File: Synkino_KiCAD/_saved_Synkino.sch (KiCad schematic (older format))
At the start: 101 parts

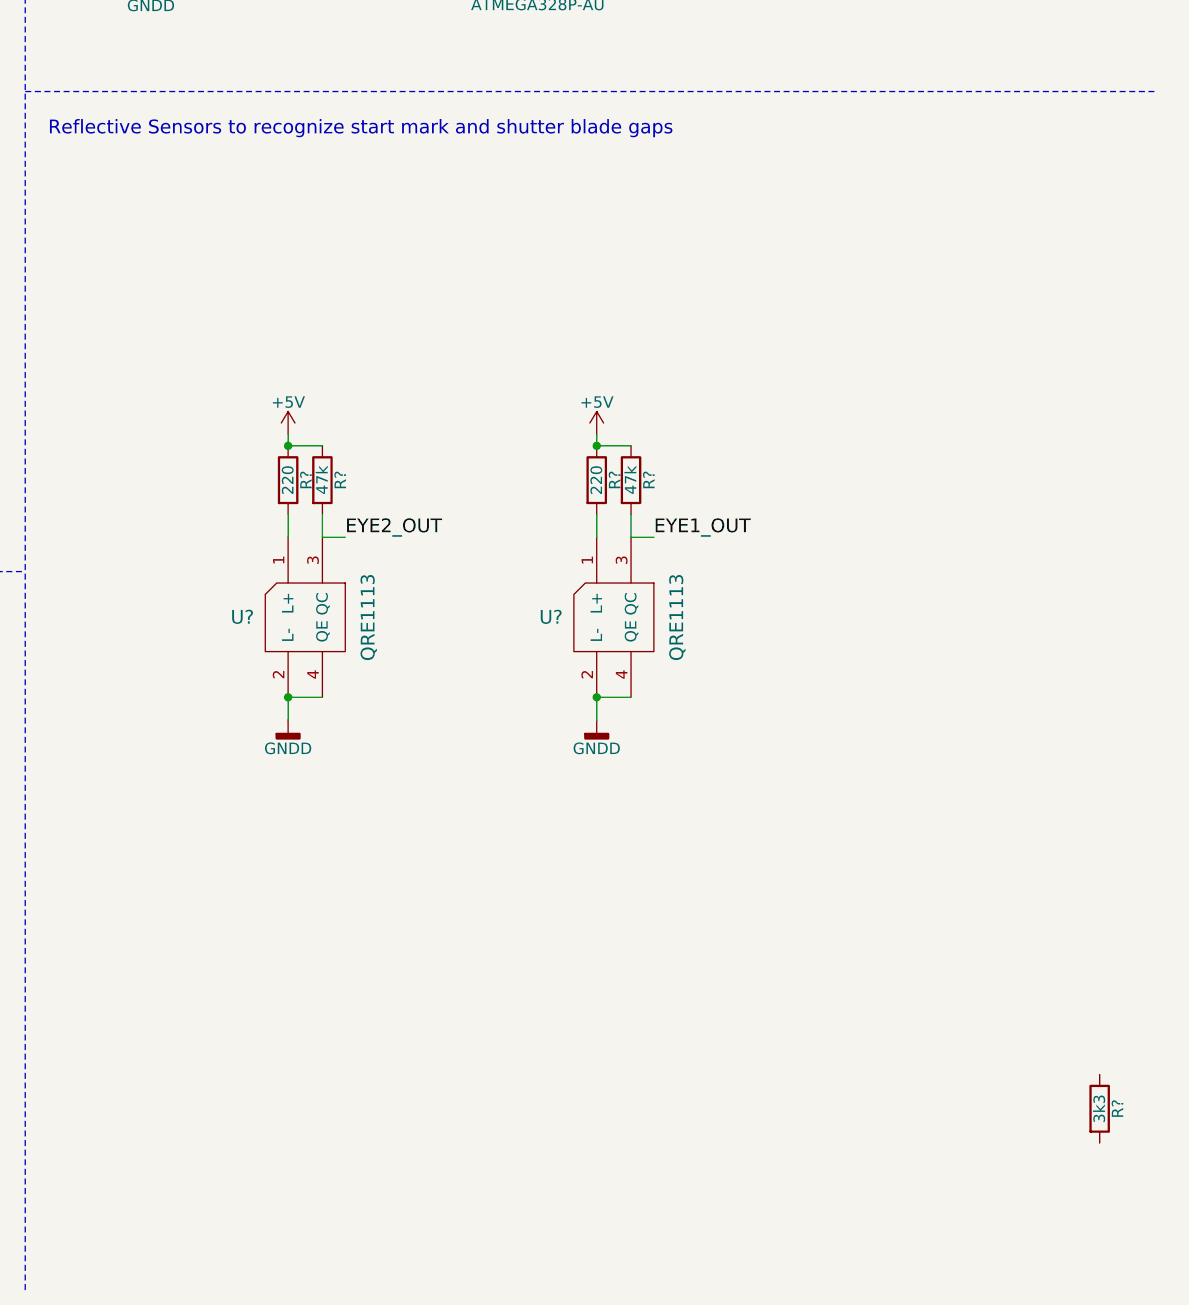
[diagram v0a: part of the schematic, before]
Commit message: Adding two Eyes
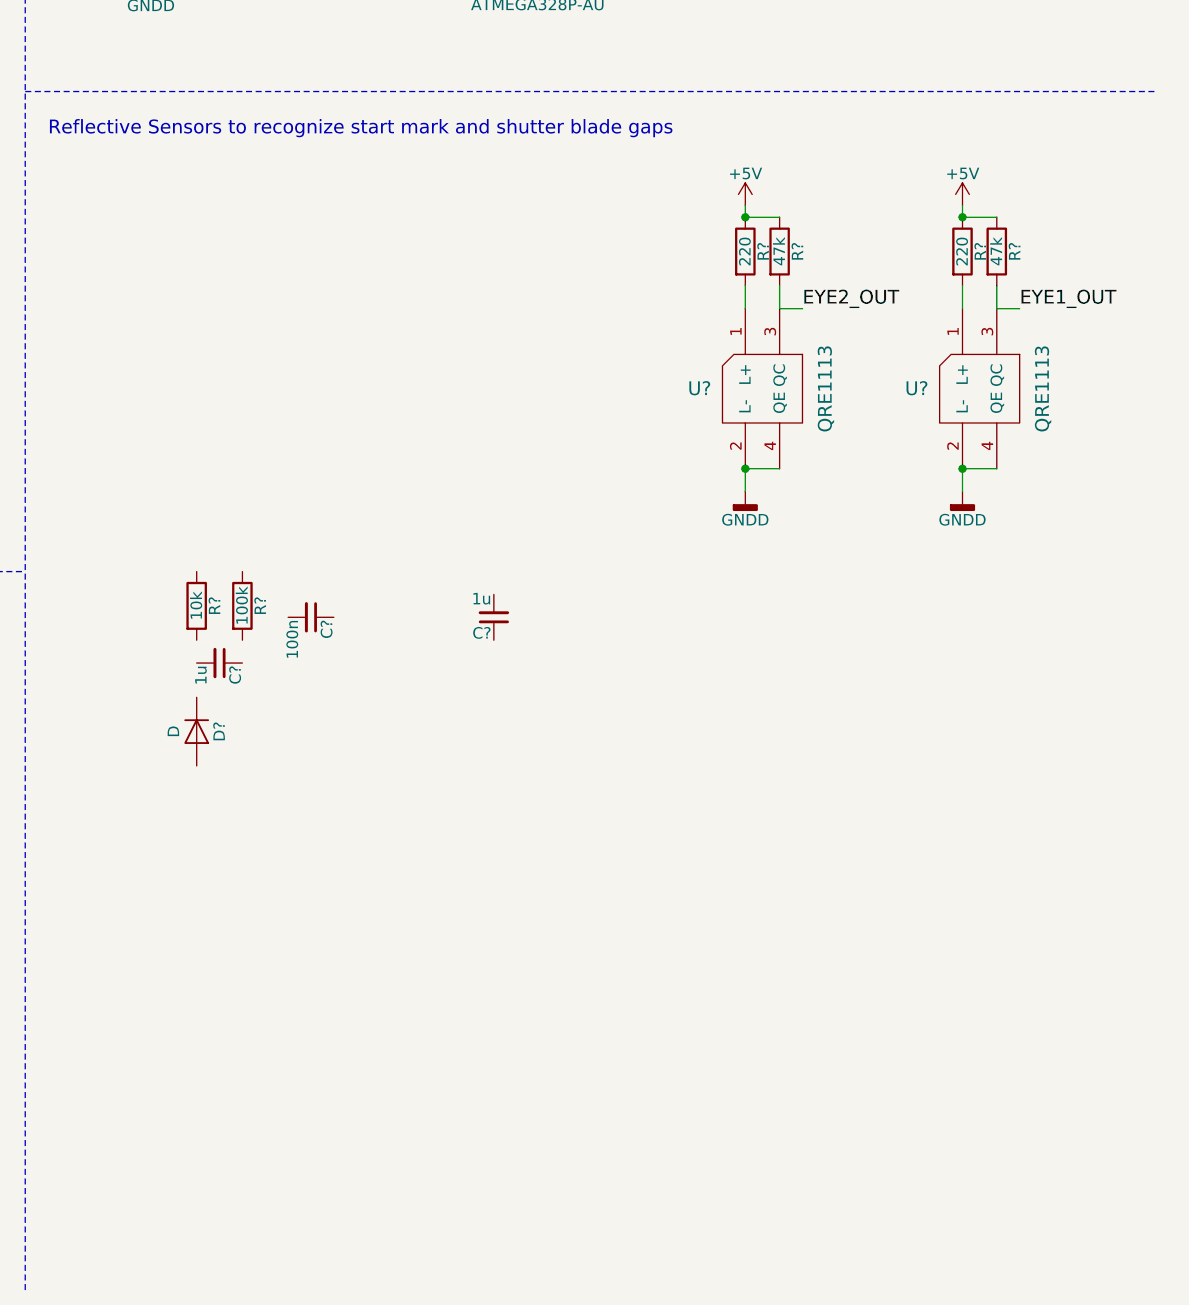
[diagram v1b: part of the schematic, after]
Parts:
- removed R?: 3k3, symbol R
- added C? (x2): 1u, symbol C_Small
- added C?: 100n, symbol C_Small
- added D?: D, symbol D
- added R?: 10k, symbol R
- added R?: 100k, symbol R
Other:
- moved on the sheet: R?, U?
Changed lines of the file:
@@
 	2200 1250 2800 1250
-$Comp
-L R R?
-U 1 1 5A9DBE51
-P 15800 10400
-F 0 "R?" V 15880 10400 50  0000 C CNN
-F 1 "3k3" V 15800 10400 50  0000 C CNN
-F 2 "" V 15730 10400 50  0001 C CNN
-F 3 "" H 15800 10400 50  0001 C CNN
-	1    15800 10400
-	1    0    0    -1
-$EndComp
 $Comp
 L QRE1113 U?
 U 1 1 5A9DC964
-P 12350 8250
-F 0 "U?" H 12050 8250 60  0000 C CNN
-F 1 "QRE1113" V 12600 8250 60  0000 C CNN
-F 2 "" V 12350 8100 60  0001 C CNN
-F 3 "" V 12350 8100 60  0001 C CNN
-	1    12350 8250
+P 14350 7250
+F 0 "U?" H 14050 7250 60  0000 C CNN
+F 1 "QRE1113" V 14600 7250 60  0000 C CNN
+F 2 "" V 14350 7100 60  0001 C CNN
+F 3 "" V 14350 7100 60  0001 C CNN
+	1    14350 7250
 	1    0    0    -1
 $EndComp
@@
 L R R?
 U 1 1 5A9DCABE
-P 12250 7650
-F 0 "R?" V 12330 7650 50  0000 C CNN
-F 1 "220" V 12250 7650 50  0000 C CNN
-F 2 "" V 12180 7650 50  0001 C CNN
-F 3 "" H 12250 7650 50  0001 C CNN
-	1    12250 7650
+P 14250 6650
+F 0 "R?" V 14330 6650 50  0000 C CNN
+F 1 "220" V 14250 6650 50  0000 C CNN
+F 2 "" V 14180 6650 50  0001 C CNN
+F 3 "" H 14250 6650 50  0001 C CNN
+	1    14250 6650
 	1    0    0    -1
 $EndComp
@@
 L R R?
 U 1 1 5A9DCFE9
-P 12400 7650
-F 0 "R?" V 12480 7650 50  0000 C CNN
-F 1 "47k" V 12400 7650 50  0000 C CNN
-F 2 "" V 12330 7650 50  0001 C CNN
-F 3 "" H 12400 7650 50  0001 C CNN
-	1    12400 7650
-	1    0    0    -1
-$EndComp
-Wire Wire Line
-	12250 7500 12400 7500
-Wire Wire Line
-	12250 7800 12250 7900
-Wire Wire Line
-	12400 7800 12400 7900
-Wire Wire Line
-	12250 8600 12400 8600
+P 14400 6650
+F 0 "R?" V 14480 6650 50  0000 C CNN
+F 1 "47k" V 14400 6650 50  0000 C CNN
+F 2 "" V 14330 6650 50  0001 C CNN
+F 3 "" H 14400 6650 50  0001 C CNN
+	1    14400 6650
+	1    0    0    -1
+$EndComp
+Wire Wire Line
+	14250 6500 14400 6500
+Wire Wire Line
+	14250 6800 14250 6900
+Wire Wire Line
+	14400 6800 14400 6900
+Wire Wire Line
+	14250 7600 14400 7600
 $Comp
 L GNDD #PWR?
 U 1 1 5A9DDEA4
-P 12250 8700
-F 0 "#PWR?" H 12250 8450 50  0001 C CNN
-F 1 "GNDD" H 12250 8575 50  0000 C CNN
-F 2 "" H 12250 8700 50  0001 C CNN
-F 3 "" H 12250 8700 50  0001 C CNN
-	1    12250 8700
-	1    0    0    -1
-$EndComp
-Wire Wire Line
-	12250 8700 12250 8600
-Connection ~ 12250 8600
-Text Label 12500 7900 0    60   ~ 0
+P 14250 7700
+F 0 "#PWR?" H 14250 7450 50  0001 C CNN
+F 1 "GNDD" H 14250 7575 50  0000 C CNN
+F 2 "" H 14250 7700 50  0001 C CNN
+F 3 "" H 14250 7700 50  0001 C CNN
+	1    14250 7700
+	1    0    0    -1
+$EndComp
+Wire Wire Line
+	14250 7700 14250 7600
+Connection ~ 14250 7600
+Text Label 14500 6900 0    60   ~ 0
 EYE2_OUT
 Wire Wire Line
-	12400 7900 12500 7900
+	14400 6900 14500 6900
 $Comp
 L +5V #PWR?
 U 1 1 5A9DE902
-P 12250 7450
-F 0 "#PWR?" H 12250 7300 50  0001 C CNN
-F 1 "+5V" H 12250 7590 50  0000 C CNN
-F 2 "" H 12250 7450 50  0001 C CNN
-F 3 "" H 12250 7450 50  0001 C CNN
-	1    12250 7450
-	1    0    0    -1
-$EndComp
-Wire Wire Line
-	12250 7450 12250 7500
-Connection ~ 12250 7500
+P 14250 6450
+F 0 "#PWR?" H 14250 6300 50  0001 C CNN
+F 1 "+5V" H 14250 6590 50  0000 C CNN
+F 2 "" H 14250 6450 50  0001 C CNN
+F 3 "" H 14250 6450 50  0001 C CNN
+	1    14250 6450
+	1    0    0    -1
+$EndComp
+Wire Wire Line
+	14250 6450 14250 6500
+Connection ~ 14250 6500
 $Comp
 L QRE1113 U?
 U 1 1 5A9DEE54
-P 13700 8250
-F 0 "U?" H 13400 8250 60  0000 C CNN
-F 1 "QRE1113" V 13950 8250 60  0000 C CNN
-F 2 "" V 13700 8100 60  0001 C CNN
-F 3 "" V 13700 8100 60  0001 C CNN
-	1    13700 8250
+P 15300 7250
+F 0 "U?" H 15000 7250 60  0000 C CNN
+F 1 "QRE1113" V 15550 7250 60  0000 C CNN
+F 2 "" V 15300 7100 60  0001 C CNN
+F 3 "" V 15300 7100 60  0001 C CNN
+	1    15300 7250
 	1    0    0    -1
 $EndComp
@@
 L R R?
 U 1 1 5A9DEE5A
-P 13600 7650
-F 0 "R?" V 13680 7650 50  0000 C CNN
-F 1 "220" V 13600 7650 50  0000 C CNN
-F 2 "" V 13530 7650 50  0001 C CNN
-F 3 "" H 13600 7650 50  0001 C CNN
-	1    13600 7650
+P 15200 6650
+F 0 "R?" V 15280 6650 50  0000 C CNN
+F 1 "220" V 15200 6650 50  0000 C CNN
+F 2 "" V 15130 6650 50  0001 C CNN
+F 3 "" H 15200 6650 50  0001 C CNN
+	1    15200 6650
 	1    0    0    -1
 $EndComp
@@
 L R R?
 U 1 1 5A9DEE60
-P 13750 7650
-F 0 "R?" V 13830 7650 50  0000 C CNN
-F 1 "47k" V 13750 7650 50  0000 C CNN
-F 2 "" V 13680 7650 50  0001 C CNN
-F 3 "" H 13750 7650 50  0001 C CNN
-	1    13750 7650
-	1    0    0    -1
-$EndComp
-Wire Wire Line
-	13600 7500 13750 7500
-Wire Wire Line
-	13600 7800 13600 7900
-Wire Wire Line
-	13750 7800 13750 7900
-Wire Wire Line
-	13600 8600 13750 8600
+P 15350 6650
+F 0 "R?" V 15430 6650 50  0000 C CNN
+F 1 "47k" V 15350 6650 50  0000 C CNN
+F 2 "" V 15280 6650 50  0001 C CNN
+F 3 "" H 15350 6650 50  0001 C CNN
+	1    15350 6650
+	1    0    0    -1
+$EndComp
+Wire Wire Line
+	15200 6500 15350 6500
+Wire Wire Line
+	15200 6800 15200 6900
+Wire Wire Line
+	15350 6800 15350 6900
+Wire Wire Line
+	15200 7600 15350 7600
 $Comp
 L GNDD #PWR?
 U 1 1 5A9DEE6A
-P 13600 8700
-F 0 "#PWR?" H 13600 8450 50  0001 C CNN
-F 1 "GNDD" H 13600 8575 50  0000 C CNN
-F 2 "" H 13600 8700 50  0001 C CNN
-F 3 "" H 13600 8700 50  0001 C CNN
-	1    13600 8700
-	1    0    0    -1
-$EndComp
-Wire Wire Line
-	13600 8700 13600 8600
-Connection ~ 13600 8600
-Text Label 13850 7900 0    60   ~ 0
+P 15200 7700
+F 0 "#PWR?" H 15200 7450 50  0001 C CNN
+F 1 "GNDD" H 15200 7575 50  0000 C CNN
+F 2 "" H 15200 7700 50  0001 C CNN
+F 3 "" H 15200 7700 50  0001 C CNN
+	1    15200 7700
+	1    0    0    -1
+$EndComp
+Wire Wire Line
+	15200 7700 15200 7600
+Connection ~ 15200 7600
+Text Label 15450 6900 0    60   ~ 0
 EYE1_OUT
 Wire Wire Line
-	13750 7900 13850 7900
+	15350 6900 15450 6900
 $Comp
 L +5V #PWR?
 U 1 1 5A9DEE74
-P 13600 7450
-F 0 "#PWR?" H 13600 7300 50  0001 C CNN
-F 1 "+5V" H 13600 7590 50  0000 C CNN
-F 2 "" H 13600 7450 50  0001 C CNN
-F 3 "" H 13600 7450 50  0001 C CNN
-	1    13600 7450
-	1    0    0    -1
-$EndComp
-Wire Wire Line
-	13600 7450 13600 7500
-Connection ~ 13600 7500
+P 15200 6450
+F 0 "#PWR?" H 15200 6300 50  0001 C CNN
+F 1 "+5V" H 15200 6590 50  0000 C CNN
+F 2 "" H 15200 6450 50  0001 C CNN
+F 3 "" H 15200 6450 50  0001 C CNN
+	1    15200 6450
+	1    0    0    -1
+$EndComp
+Wire Wire Line
+	15200 6450 15200 6500
+Connection ~ 15200 6500
 Text Notes 11200 6150 0    60   ~ 0
 Reflective Sensors to recognize start mark and shutter blade gaps
+$Comp
+L R R?
+U 1 1 5A9E21D5
+P 11850 8200
+F 0 "R?" V 11930 8200 50  0000 C CNN
+F 1 "10k" V 11850 8200 50  0000 C CNN
+F 2 "" V 11780 8200 50  0001 C CNN
+F 3 "" H 11850 8200 50  0001 C CNN
+	1    11850 8200
+	1    0    0    -1
+$EndComp
+$Comp
+L R R?
+U 1 1 5A9E2416
+P 12050 8200
+F 0 "R?" V 12130 8200 50  0000 C CNN
+F 1 "100k" V 12050 8200 50  0000 C CNN
+F 2 "" V 11980 8200 50  0001 C CNN
+F 3 "" H 12050 8200 50  0001 C CNN
+	1    12050 8200
+	1    0    0    -1
+$EndComp
+$Comp
+L C_Small C?
+U 1 1 5A9E2637
+P 11950 8450
+F 0 "C?" H 11960 8520 50  0000 L CNN
+F 1 "1u" H 11960 8370 50  0000 L CNN
+F 2 "" H 11950 8450 50  0001 C CNN
+F 3 "" H 11950 8450 50  0001 C CNN
+	1    11950 8450
+	0    1    1    0
+$EndComp
+$Comp
+L D D?
+U 1 1 5A9E2CC0
+P 11850 8750
+F 0 "D?" H 11850 8850 50  0000 C CNN
+F 1 "D" H 11850 8650 50  0000 C CNN
+F 2 "" H 11850 8750 50  0001 C CNN
+F 3 "" H 11850 8750 50  0001 C CNN
+	1    11850 8750
+	0    1    1    0
+$EndComp
+$Comp
+L C_Small C?
+U 1 1 5A9E2E2A
+P 12350 8250
+F 0 "C?" H 12360 8320 50  0000 L CNN
+F 1 "100n" H 12360 8170 50  0000 L CNN
+F 2 "" H 12350 8250 50  0001 C CNN
+F 3 "" H 12350 8250 50  0001 C CNN
+	1    12350 8250
+	0    1    1    0
+$EndComp
+$Comp
+L C_Small C?
+U 1 1 5A9E30F5
+P 13150 8250
+F 0 "C?" H 13160 8320 50  0000 L CNN
+F 1 "1u" H 13160 8170 50  0000 L CNN
+F 2 "" H 13150 8250 50  0001 C CNN
+F 3 "" H 13150 8250 50  0001 C CNN
+	1    13150 8250
+	-1   0    0    1
+$EndComp
 $EndSCHEMATC
